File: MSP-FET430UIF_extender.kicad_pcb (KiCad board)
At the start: 2 copper layers, 39.1 x 26.4 mm, 8 parts, among them P1 CONN_01X03, P2 CONN_02X07, P3 CONN_01X02, P4 CONN_01X08

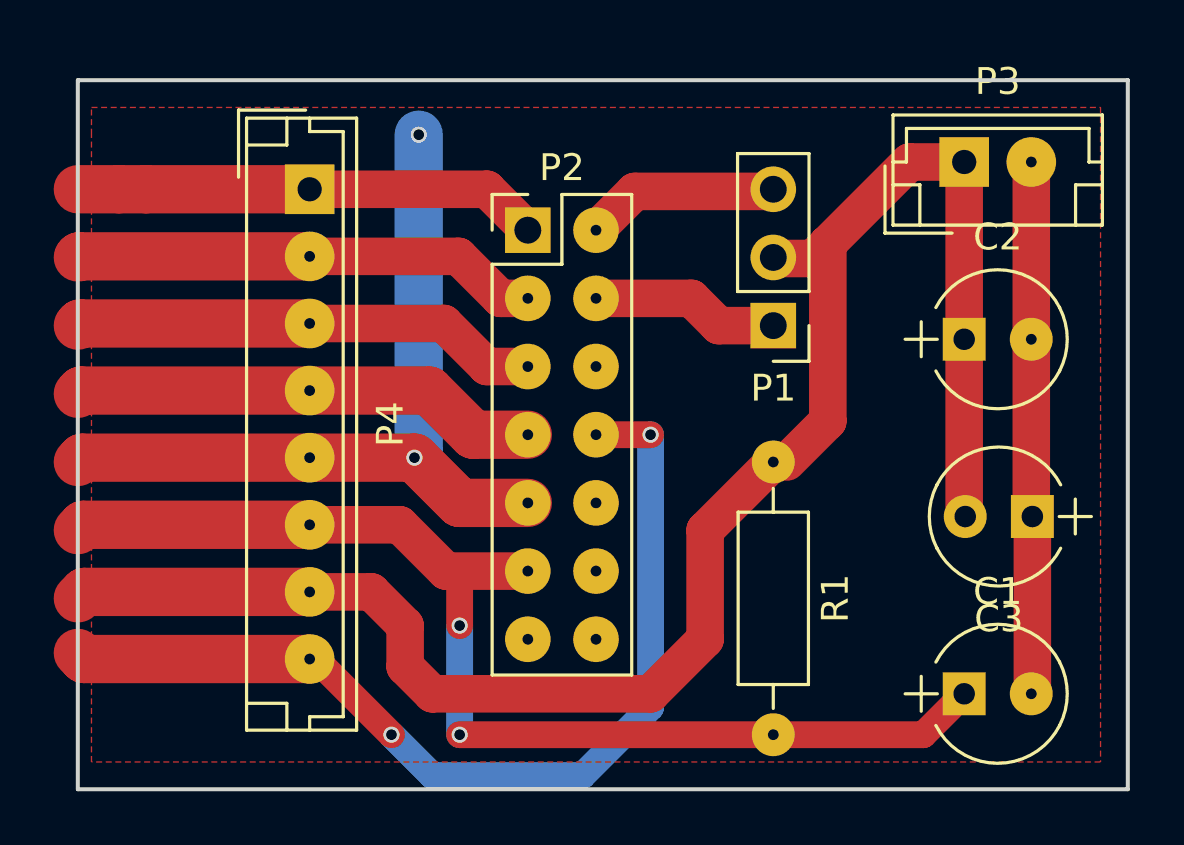
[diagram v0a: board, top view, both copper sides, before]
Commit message: *remapping sysmbol into latest version of kicad
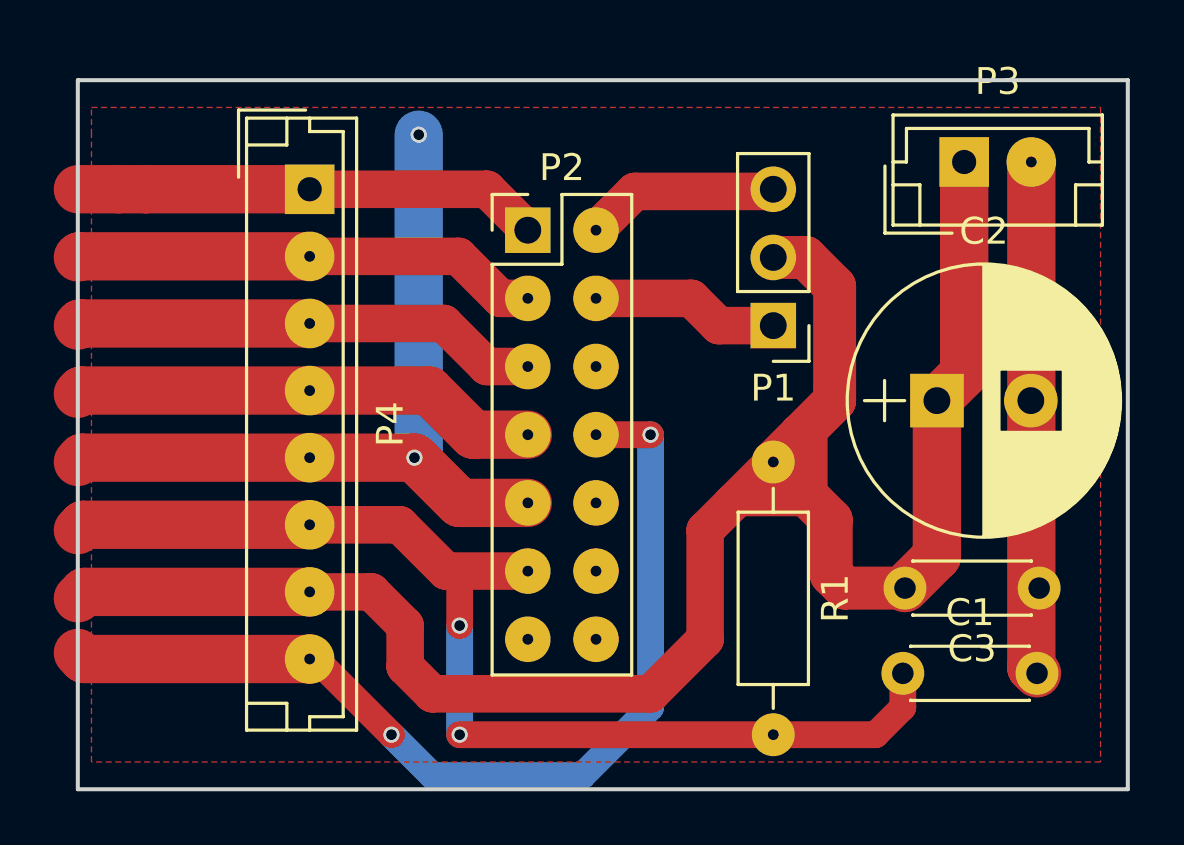
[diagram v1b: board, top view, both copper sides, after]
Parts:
- C1, C3: footprint Capacitors_ThroughHole:CP_Radial_Tantal_D5.0mm_P2.50mm -> Capacitors_ThroughHole:C_Disc_D4.3mm_W1.9mm_P5.00mm
- C2: footprint Capacitors_ThroughHole:CP_Radial_Tantal_D5.0mm_P2.50mm -> Capacitors_ThroughHole:CP_Radial_D10.0mm_P3.50mm
- moved C3 2.68 mm to (166.4, 117.5)
- moved C2 2.50 mm to (162.6, 110.5)
- moved C1 2.41 mm to (161.3, 120.7)
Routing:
- net /VCC: track 65.5 -> 79.5 mm
- net /RST: track 45.6 -> 44.4 mm
- net /GND: track 51.9 -> 51.1 mm
